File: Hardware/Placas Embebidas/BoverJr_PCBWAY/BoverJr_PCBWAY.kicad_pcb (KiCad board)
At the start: 2 copper layers, 100 x 100.1 mm, 51 parts, among them J1 Encoder Derecho, J10 7.4v, J11 Cable_PAD, J2 Encoder Izquierdo, J3 Programador, J4 Distancia_Der, J5 Distancia_Izq, J6 Cable_PAD, J7 Cable_PAD, J8 Distancia_Frontal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

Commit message: Para mi esat lista , verificada por 3D y ezequiel, faltaria saber que dice bustos
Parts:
- removed the ? at (111.0, 53.0)
- removed the ? at (136.0, 34.5)
- removed the ? at (189.0, 53.0)
- removed the ? at (164.0, 34.5)
- added ?: , , F.Cu at (111.0, 53.0)
- added ?: , , F.Cu at (189.0, 53.0)
- added ?: , , F.Cu at (136.0, 34.4)
- added ?: , , F.Cu at (164.0, 34.5)
- added G8: LOGO_ROTULO, EESTN5:LOGO_EESTN5_F.Cu, F.Cu at (136.0, 83.8)
- R1, R2, R3, R7, R8: footprint EESTN5:R_1206 -> EESTN5:R_0805
- moved J8 2.77 mm to (167.1, 42.1), turned to 180 degrees
- moved SW1 2.56 mm to (108.7, 87.2)
- turned R1 to 90 degrees
- turned R2 to -90 degrees
- turned R3 to -90 degrees
- turned R7 to 90 degrees
- turned R8 to 180 degrees
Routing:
- net GND: track 39.1 -> 27.6 mm
- net +5V: track 206.3 -> 200.4 mm
- net VCC: track 102.2 -> 98.8 mm
- net /IR_FRONTAL: track 8.71 -> 5.66 mm
- net +BATT: track 8.72 -> 11.2 mm
- net +3.3V: track 277.6 -> 277.0 mm

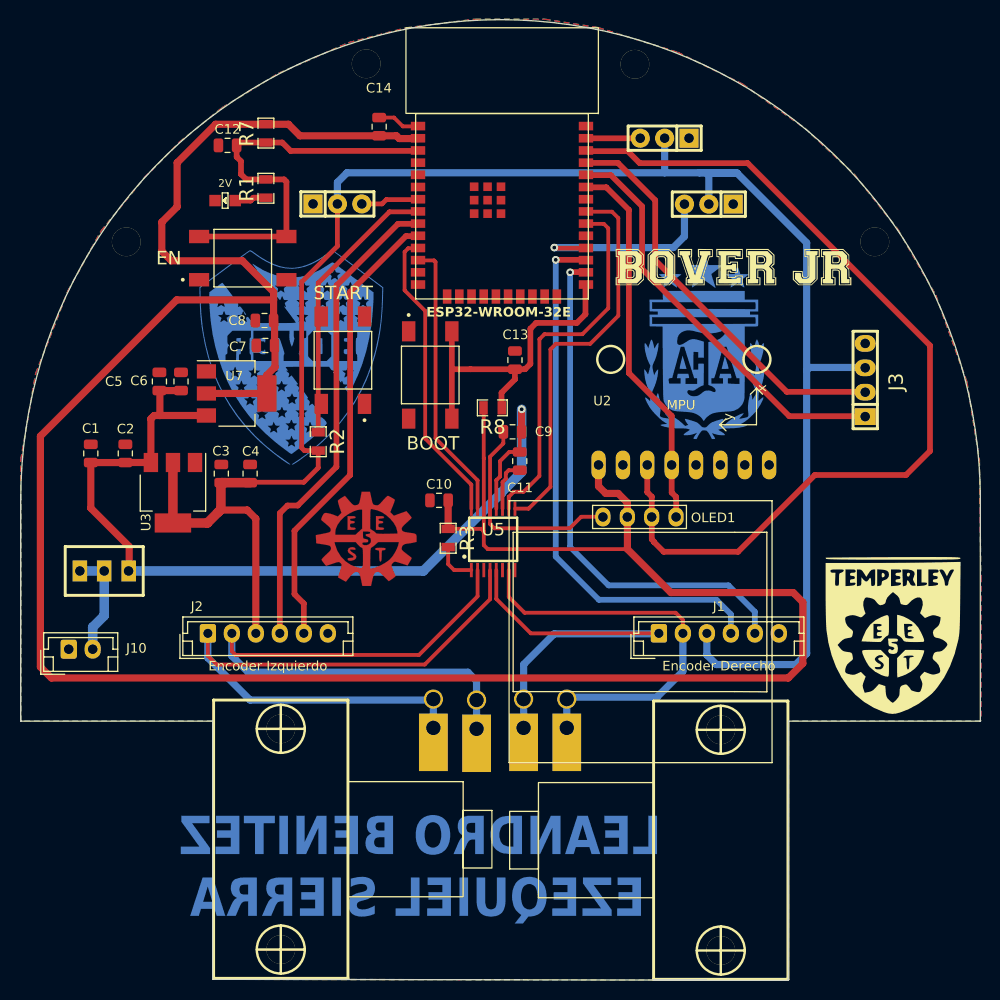
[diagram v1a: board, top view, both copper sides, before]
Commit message: retoques en la seligrafia para que quede mejor
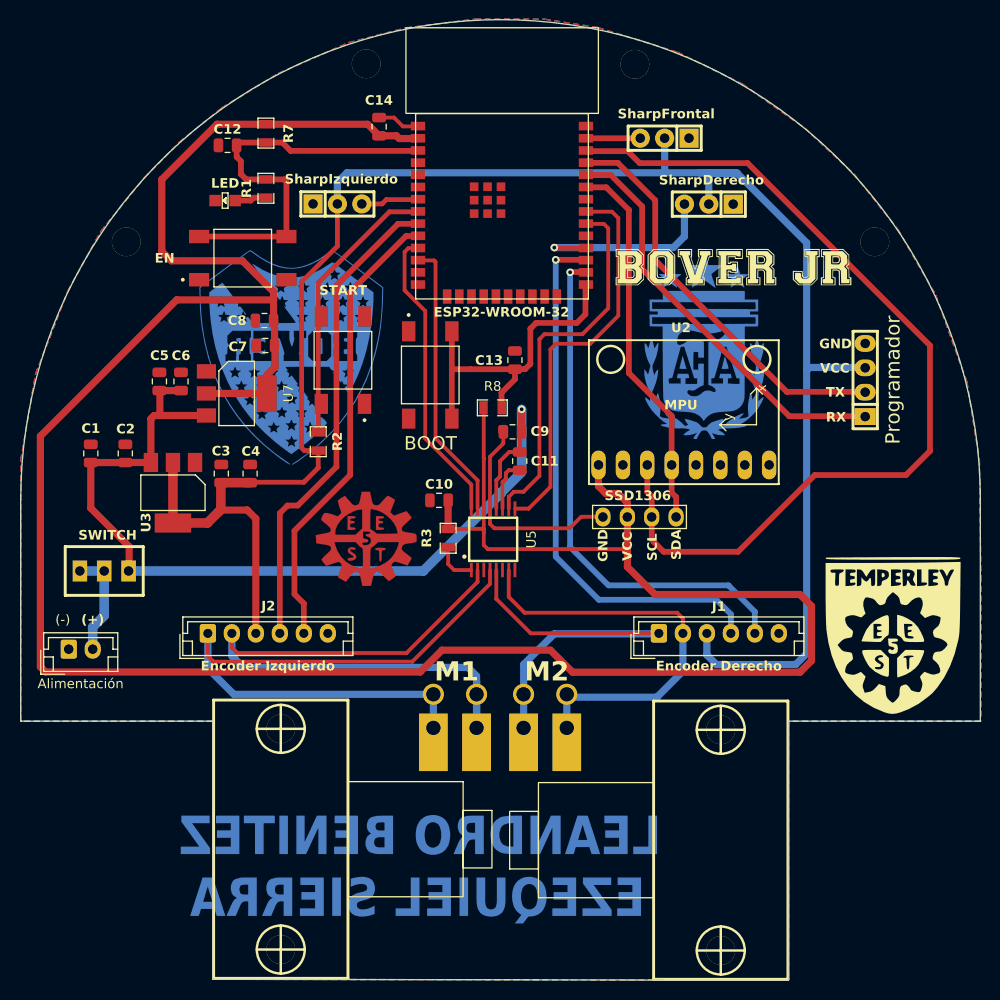
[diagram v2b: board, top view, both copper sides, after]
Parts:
- LED_ESP32: value 2V -> LED
- U1: value ESP32-WROOM-32E -> ESP32-WROOM-32
- moved J11 0.10 mm to (147.5, 103.6)
- renumbered J3 to Programador, OLED1 to SSD1306
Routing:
- net /OUT_B_MOTOR2: track 69.6 -> 73.5 mm
- net +3.3V: track 277.0 -> 280.8 mm
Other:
- outline, holes or cut-outs redrawn
- board text added: "(+)"
- board text added: "(-)"
- board text added: "GND"
- board text added: "M1"
- board text added: "M2"
- board text added: "RX"
- board text added: "SCL"
- board text added: "SDA"
- board text added: "SWITCH"
- board text added: "SharpDerecho"
- board text added: "SharpFrontal"
- board text added: "SharpIzquierdo"
- board text added: "TX"
- board text added: "VCC"

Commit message: cosas por mejorar
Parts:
- removed G8: LOGO_ROTULO, EESTN5:LOGO_EESTN5_F.Cu
- added G10: LOGO, EESTN5:Leandro, F.Cu at (129.1, 87.8)
- added G11: LOGO, EESTN5:ezequiel, F.Cu at (129.1, 84.8)
- J3: renamed from Programador; value Programador -> Programmer; footprint EESTN5:pin_strip_4 -> Connector_PinSocket_2.54mm:PinSocket_1x04_P2.54mm_Vertical
- J4, J5, J8: footprint EESTN5:Pin_Strip_3 -> Connector_JST:JST_XH_B3B-XH-AM_1x03_P2.50mm_Vertical
- LED_ESP32: value LED -> 2V
- U1: value ESP32-WROOM-32 -> ESP32-WROOM-32E
- moved C10 11.5 mm to (154.4, 83.8), turned to -90 degrees
- moved J3 3.75 mm to (187.9, 71.1), turned to 180 degrees
- moved J8 3.01 mm to (169.6, 40.4)
- moved J4 2.50 mm to (174.2, 49.2)
- moved J5 1.85 mm to (131.2, 49.0)
- moved SW_EN1 1.19 mm to (122.0, 54.6)
- renumbered SSD1306 to OLED1
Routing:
- net +5V: track 200.4 -> 202.4 mm
- net /IR_FRONTAL: track 5.66 -> 7.18 mm
- net +3.3V: track 280.8 -> 279.6 mm
- net /IR_DER: track 6.05 -> 5.53 mm
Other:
- board text added: "Front Sensor"
- board text added: "Left Sensor"
- board text added: "Right Sensor"
- board text removed: "SharpDerecho"
- board text removed: "SharpFrontal"
- board text removed: "SharpIzquierdo"

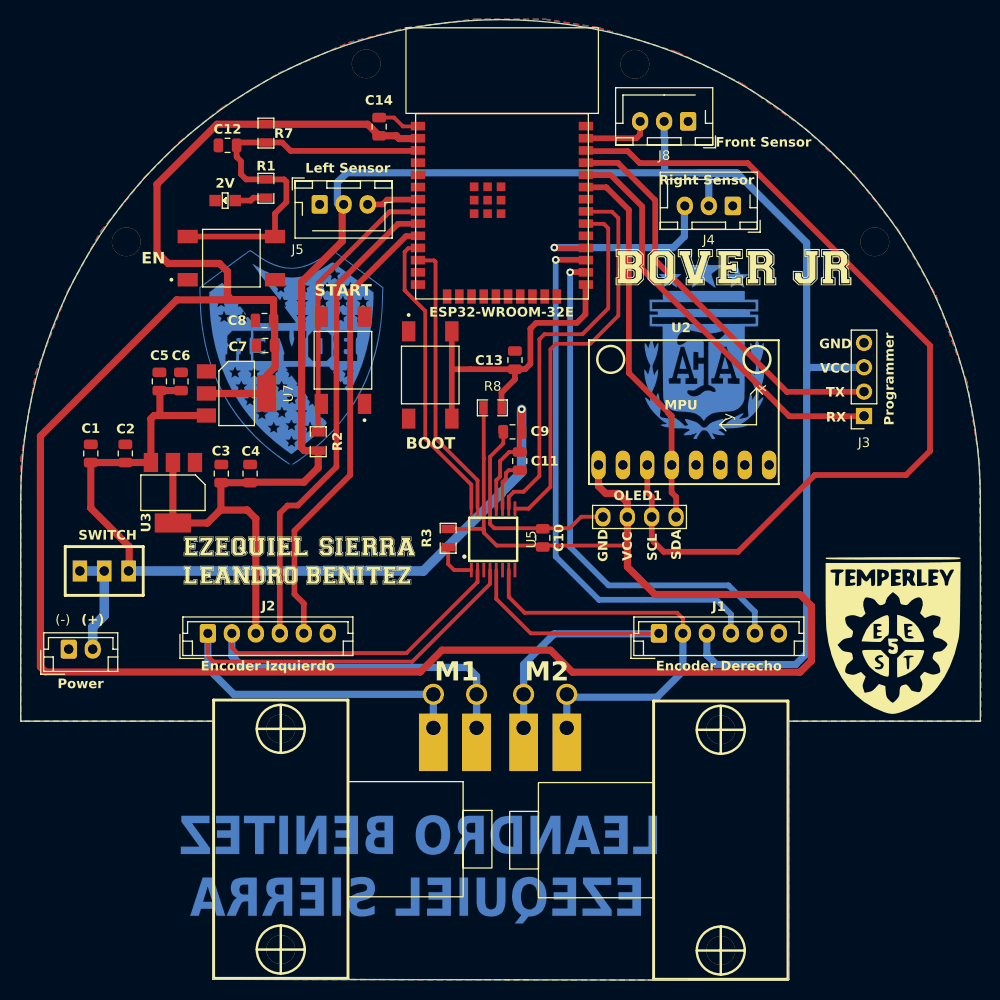
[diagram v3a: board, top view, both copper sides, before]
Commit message: para mi ya esta listimisima, cambie sw y agregue jst , verifique serigrafia y 3d
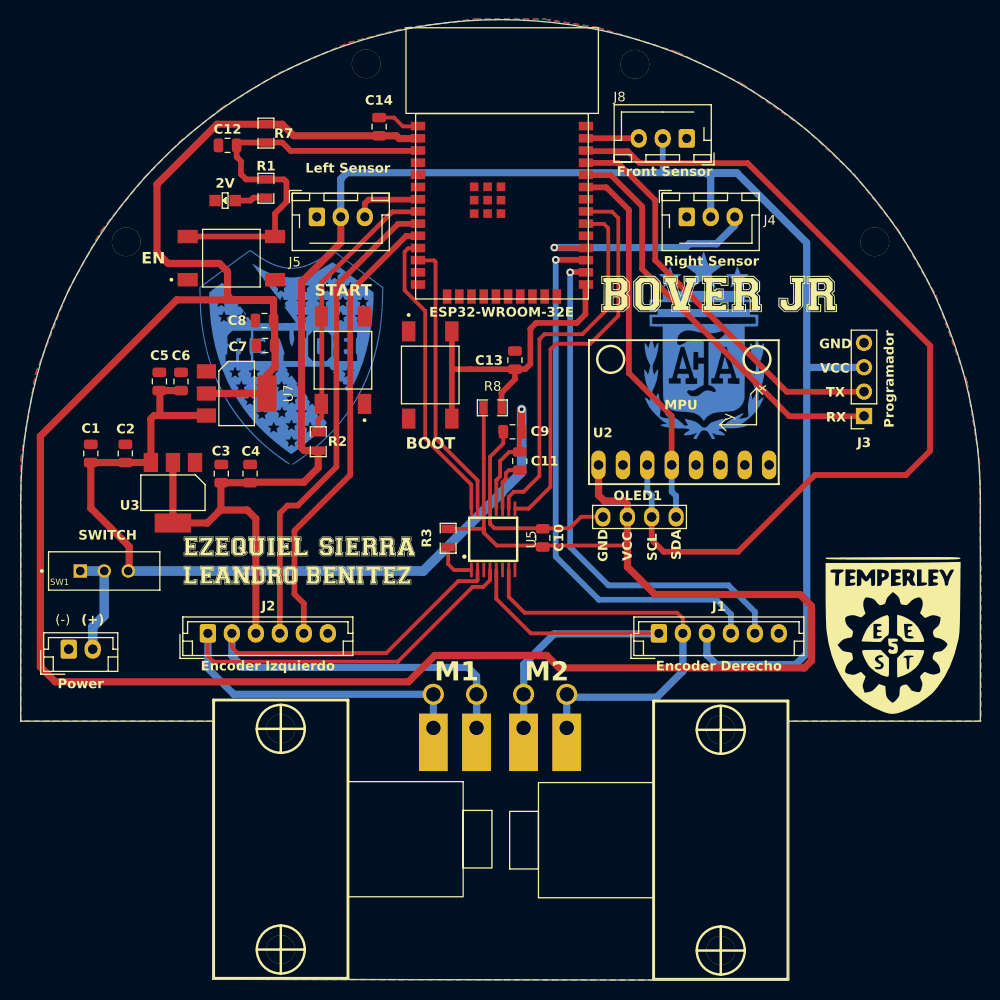
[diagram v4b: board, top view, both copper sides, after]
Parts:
- ?: moved to B.Cu
- J3: value Programmer -> Programador
- SW1: footprint EESTN5:SW_SPDT_TH_100Mils_VERTICAL -> EESTN5:SW_MINI-SPDT-SW
- moved J4 4.94 mm to (169.4, 50.4), turned to 0 degrees
- moved G6 3.18 mm to (172.8, 58.9)
- moved J8 1.78 mm to (169.4, 42.2)
- moved J5 1.33 mm to (130.8, 50.4)
- turned ? to 180 degrees
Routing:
- net /IR_IZQ: track 20.7 -> 24.0 mm
- net /IR_FRONTAL: track 7.18 -> 5.50 mm
- net /IR_DER: track 5.53 -> 7.12 mm
- net +5V: track 202.4 -> 201.9 mm
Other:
- board text removed: "LEANDRO BENITEZ EZEQUIEL SIERRA"
